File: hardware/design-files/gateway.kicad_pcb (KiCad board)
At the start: 2 copper layers, 100 x 70 mm, 0 parts

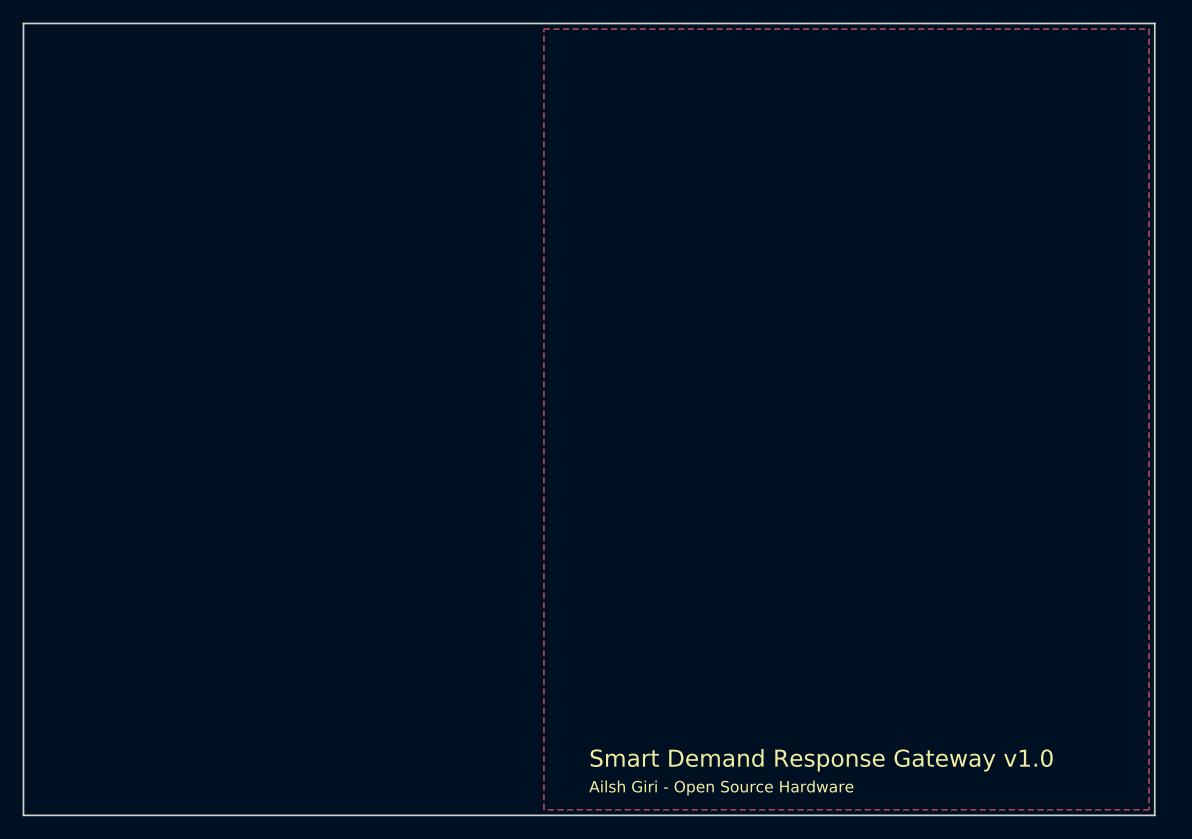
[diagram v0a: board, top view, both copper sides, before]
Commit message: feat(hardware): update KiCad schematics with component symbols and layout refinements
- Add ADS1115 16-bit I2C ADC symbol to CT sensor schematic
- Add AudioJack2 connector symbol for analog signal input
- Update ESP32 module schematic with refined pin configurations
- Update power supply schematic with improved component placement
- Update relay driver schematic with optimized routing
- Refine PCB layout in gateway.kicad_pcb with better trace routing
- Update project settings in gateway.kicad_pro for design rule compliance
- Add project rules configuration in gateway.kicad_prl for manufacturing constraints
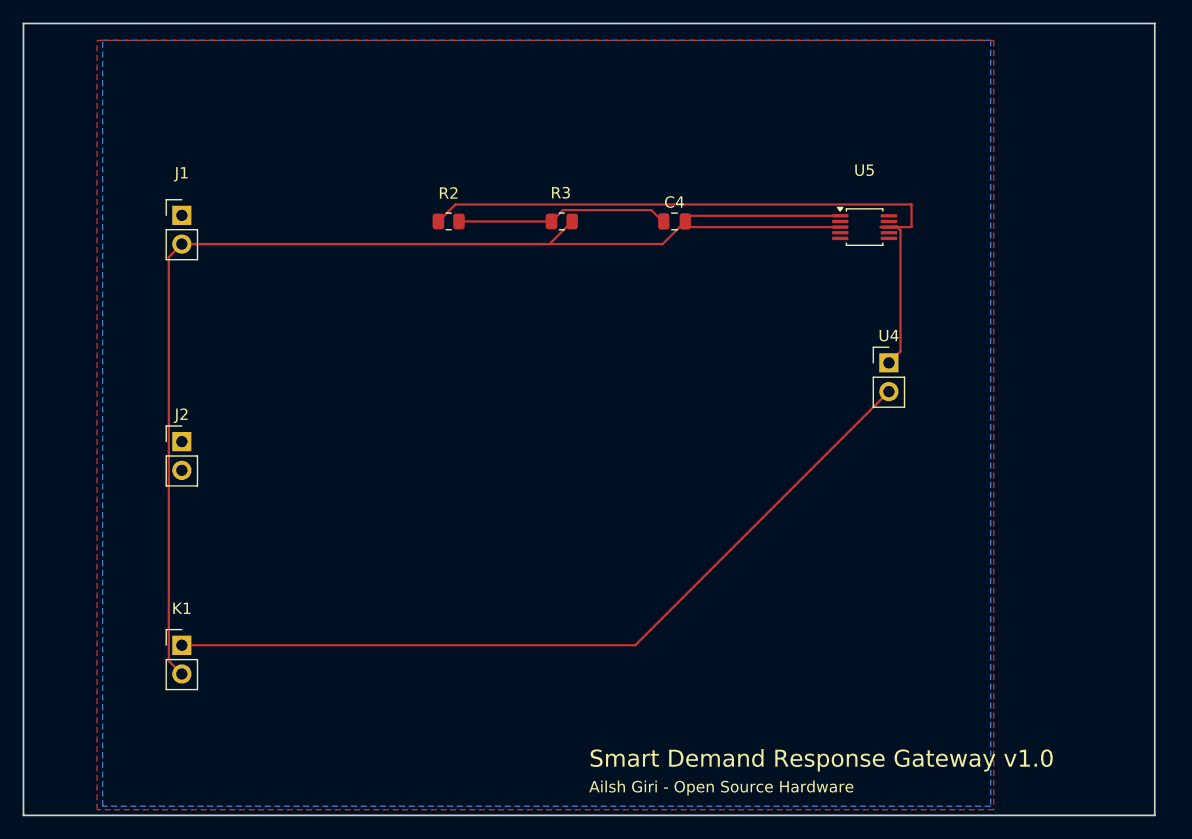
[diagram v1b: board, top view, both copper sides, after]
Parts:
- added C4: 10uF, Capacitor_SMD:C_0805_2012Metric, F.Cu at (67.5, 27.5)
- added J1: Conn_01x02, Connector_PinHeader_2.54mm:PinHeader_1x02_P2.54mm_Vertical, F.Cu at (24.0, 27.0)
- added J2: SCT-013-030, Connector_PinHeader_2.54mm:PinHeader_1x02_P2.54mm_Vertical, F.Cu at (24.0, 47.0)
- added K1: Screw_Terminal_01x04, Connector_PinHeader_2.54mm:PinHeader_1x02_P2.54mm_Vertical, F.Cu at (24.0, 65.0)
- added R2: 10K 1%, Resistor_SMD:R_0805_2012Metric, F.Cu at (47.6, 27.5)
- added R3: 10K 1%, Resistor_SMD:R_0805_2012Metric, F.Cu at (57.6, 27.5)
- added U4: ESP32 DevKit, Connector_PinHeader_2.54mm:PinHeader_1x02_P2.54mm_Vertical, F.Cu at (86.5, 40.0)
- added U5: ADS1115IDGS, Package_SO:TSSOP-10_3x3mm_P0.5mm, F.Cu at (84.3, 28.0)
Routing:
- net GND: track 0.00 -> 147.4 mm
- net /ESP32 DEVKITV1 Module/GND: track 0.00 -> 71.8 mm
- net +3.3V: track 0.00 -> 60.0 mm
- net Net-(C4-Pad1): track 0.00 -> 18.9 mm

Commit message: feat(hardware): update PCB layout and component footprints
- Reposition ADS1115 ADC module on PCB (moved from 84.35,28 to 60.5,49.35 with 180° rotation)
- Update CT sensor connector footprint from PinHeader to 3.5mm audio jack (Switronic ST-005-G)
- Correct ESP32 module connector footprint from 1x02 to 1x06 pin header
- Regenerate component UUIDs and silk screen coordinates to reflect new placements
- Optimize PCB layout for improved signal routing and component accessibility
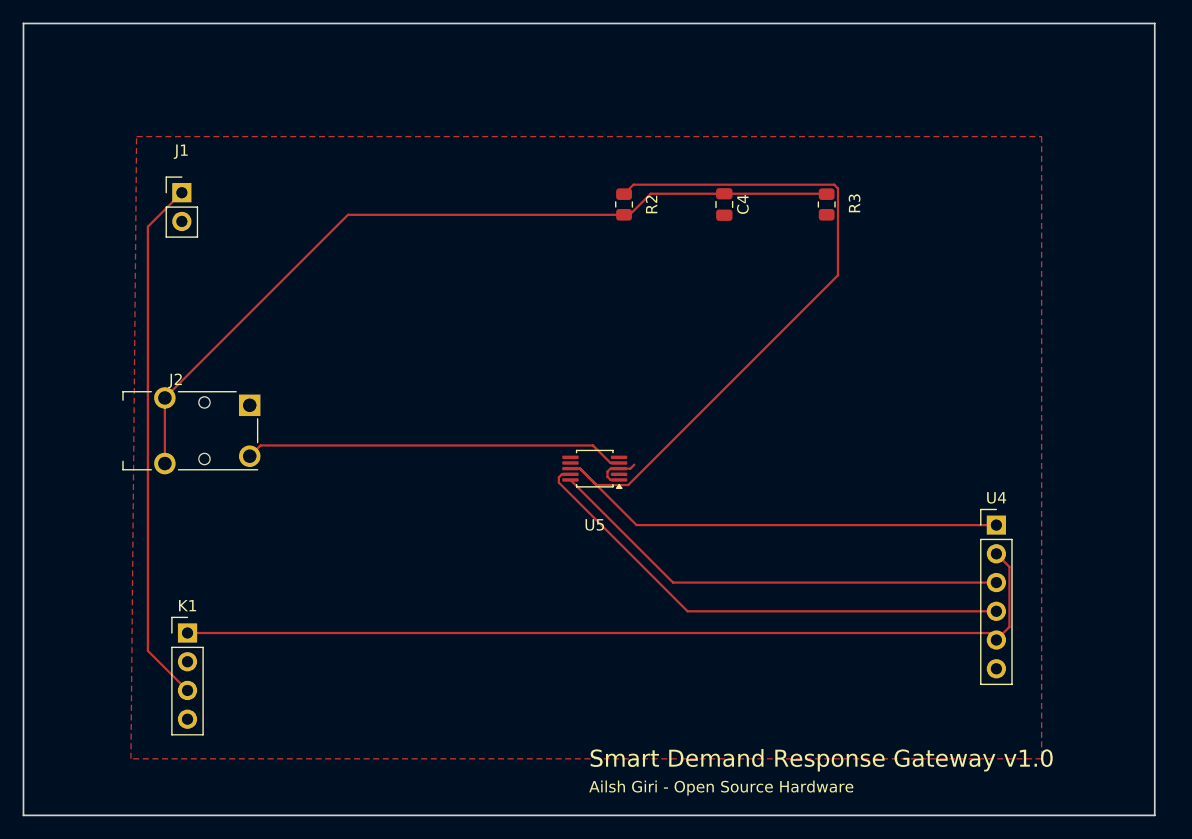
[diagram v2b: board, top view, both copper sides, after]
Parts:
- J2: footprint Connector_PinHeader_2.54mm:PinHeader_1x02_P2.54mm_Vertical -> Connector_Audio:Jack_3.5mm_Switronic_ST-005-G_horizontal
- K1: footprint Connector_PinHeader_2.54mm:PinHeader_1x02_P2.54mm_Vertical -> Connector_PinHeader_2.54mm:PinHeader_1x04_P2.54mm_Vertical
- U4: footprint Connector_PinHeader_2.54mm:PinHeader_1x02_P2.54mm_Vertical -> Connector_PinHeader_2.54mm:PinHeader_1x06_P2.54mm_Vertical
- moved U5 32.0 mm to (60.5, 49.4), turned to 180 degrees
- moved R3 23.5 mm to (81.0, 26.0), turned to -90 degrees
- moved U4 17.2 mm to (96.0, 54.3)
- moved R2 15.6 mm to (63.1, 26.0), turned to -90 degrees
- moved C4 4.65 mm to (72.0, 26.0), turned to -90 degrees
- moved J1 2.00 mm to (24.0, 25.0)
- moved K1 1.19 mm to (24.5, 63.9)
- moved J2 1.08 mm to (23.5, 46.0)
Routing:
- net GND: track 147.4 -> 4.23 mm
- net Net-(C4-Pad1): track 18.9 -> 71.8 mm
- net +5V: track 0.00 -> 46.7 mm
- net /CT Sensor Interface/I2C_SDA: track 0.00 -> 45.0 mm
- net /CT Sensor Interface/I2C_SCL: track 0.00 -> 41.4 mm
- net +3.3V: track 60.0 -> 97.9 mm
- net Net-(U5-AIN0): track 0.00 -> 33.7 mm
- net /ESP32 DEVKITV1 Module/GND: track 71.8 -> 80.3 mm
- removed copper zone on B.Cu, net GND

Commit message: feat(app,hardware): update dashboard precision and refine PCB layout
- Increase grid load watts display precision from 1 to 2 decimal places in dashboard
- Add PCB stackup configuration with FR4 dielectric specifications and copper layer thickness
- Reposition TSSOP-10 ADS1115 ADC footprint for improved layout optimization
- Relocate 0805 capacitor and resistor components for better signal integrity
- Reposition 3.5mm audio jack connector (SCT-013-030 current sensor)
- Reposition pin header connector for optimized board routing
- Update all affected component UUIDs to reflect new placements
- Regenerate PCB render documentation and Gerber fabrication files for v1.0
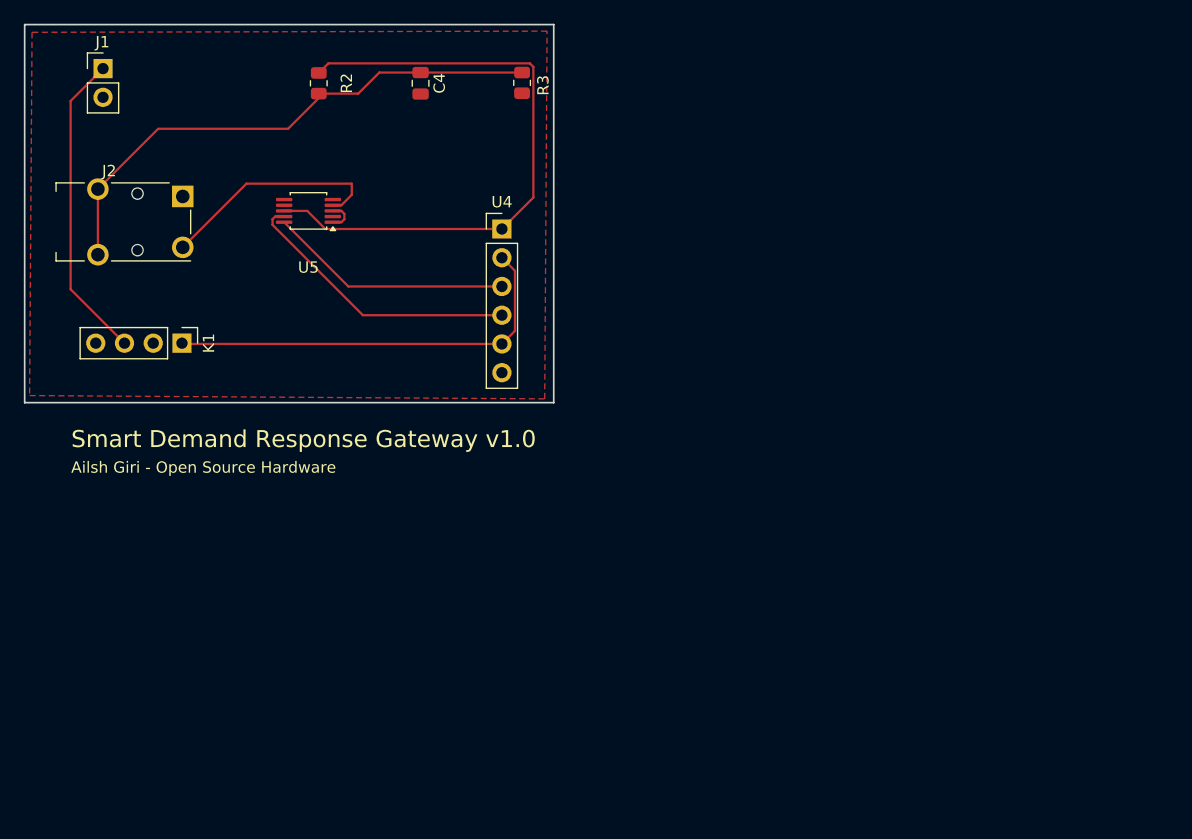
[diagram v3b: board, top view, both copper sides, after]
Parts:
- moved U4 50.9 mm to (52.3, 28.2)
- moved U5 34.1 mm to (35.2, 26.6)
- moved R2 29.0 mm to (36.1, 15.3)
- moved R3 29.0 mm to (54.1, 15.2)
- moved C4 28.9 mm to (45.1, 15.3)
- moved K1 25.6 mm to (24.0, 38.3), turned to -90 degrees
- moved J2 19.4 mm to (17.6, 27.5)
- moved J1 13.0 mm to (17.0, 14.0)
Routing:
- net /ESP32 DEVKITV1 Module/GND: track 80.3 -> 36.9 mm
- net +3.3V: track 97.9 -> 54.8 mm
- net Net-(C4-Pad1): track 71.8 -> 47.8 mm
- net /CT Sensor Interface/I2C_SCL: track 41.4 -> 21.6 mm
- net /CT Sensor Interface/I2C_SDA: track 45.0 -> 25.2 mm
- net +5V: track 46.7 -> 27.4 mm
- net Net-(U5-AIN0): track 33.7 -> 20.3 mm
- net GND: track 4.23 -> 2.74 mm
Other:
- board size 100 x 70 mm -> 46.8 x 33.4 mm
